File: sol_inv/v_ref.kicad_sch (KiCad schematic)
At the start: 3 parts, among them U7 LM4040DIM3-2.5, U8 MCP6001-OT

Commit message: v0.2 components change + reference to providers
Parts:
- R15: ComponentLink2URL (none) -> https://ro.farnell.com/yageo/rt0603bre078kl/res-8k-0-1-0-1w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
- U7: ComponentLink2URL (none) -> https://ro.farnell.com/texas-instruments/lm4040dim3-2-5-nop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
- U8: ComponentLink2URL (none) -> https://ro.mouser.com/ProductDetail/Microchip-Technology/MC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
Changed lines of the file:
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@@
 	(title_block
 		(title "Voltage Reference for ADC")
-		(date "2025-03-13")
-		(rev "0.1")
+		(date "2025-04-10")
+		(rev "0.2")
 		(company "Cezar-Octavian Bontaș")
 	)
@@
 			)
 		)
-		(property "Datasheet" "~"
+		(property "Datasheet" "https://www.yageo.com/upload/media/product/app/datasheet/rchip/pyu-rt_1-to-0.01_rohs_l.pdf"
 			(at 130.81 91.44 0)
 			(effects
@@
 		)
 		(property "Description" "Resistor"
+			(at 130.81 91.44 0)
+			(effects
+				(font
+					(size 1.27 1.27)
+				)
+				(hide yes)
+			)
+		)
+		(property "ComponentLink1URL" ""
+			(at 130.81 91.44 0)
+			(effects
+				(font
+					(size 1.27 1.27)
+				)
+			)
+		)
+		(property "ComponentLink2URL" "https://ro.farnell.com/yageo/rt0603bre078kl/res-8k-0-1-0-1w-thin-film-0603/dp/4148462"
 			(at 130.81 91.44 0)
 			(effects
@@
 			)
 		)
+		(property "ComponentLink1URL" ""
+			(at 130.81 106.68 0)
+			(effects
+				(font
+					(size 1.27 1.27)
+				)
+			)
+		)
+		(property "ComponentLink2URL" "https://ro.farnell.com/texas-instruments/lm4040dim3-2-5-nopb/volt-ref-shunt-2-5v-sot-23/dp/3009222"
+			(at 130.81 106.68 0)
+			(effects
+				(font
+					(size 1.27 1.27)
+				)
+				(hide yes)
+			)
+		)
 		(pin "2"
 		)
@@
 			(at 148.59 101.6 0)
 			(effects
+				(font
+					(size 1.27 1.27)
+				)
+				(hide yes)
+			)
+		)
+		(property "ComponentLink1URL" ""
+			(at 148.59 101.6 0)
+			(effects
+				(font
+					(size 1.27 1.27)
+				)
+			)
+		)
+		(property "ComponentLink2URL" "https://ro.mouser.com/ProductDetail/Microchip-Technology/MCP6001T-I-OT?qs=Q%2Fw7XRh99iki9dglS7IqJg%3D%3D"
+			(at 148.59 101.6 0)
+			(effects

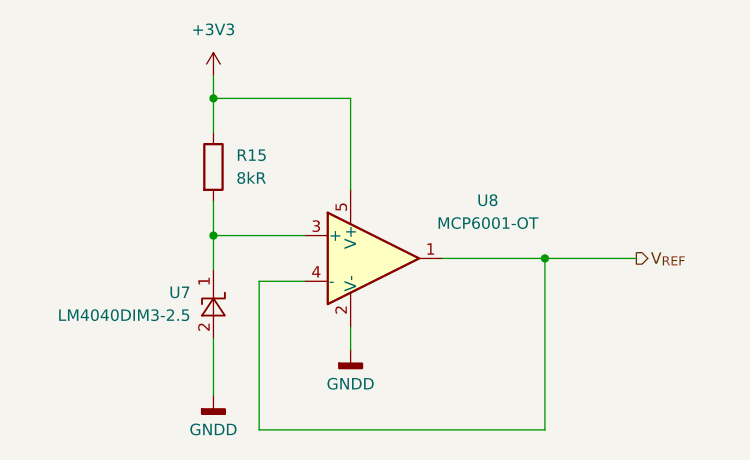
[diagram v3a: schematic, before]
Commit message: v0.3.4 fixes + component change for farnell
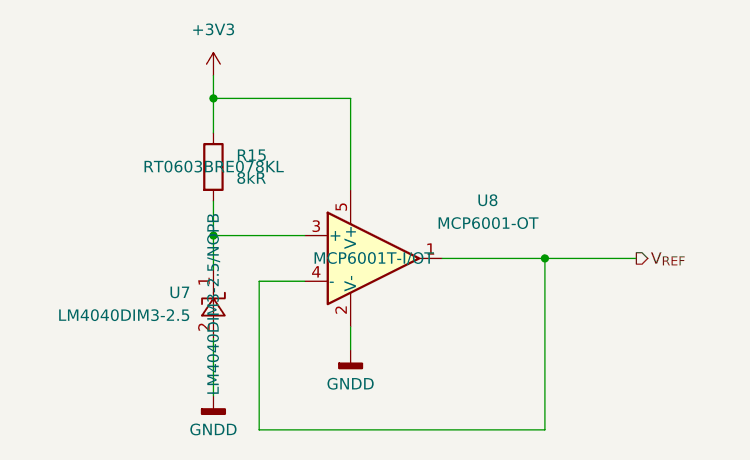
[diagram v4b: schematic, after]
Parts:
- R15: Manufacturer Part Number (none) -> RT0603BRE078KL
- U7: Manufacturer Part Number (none) -> LM4040DIM3-2.5/NOPB
- U8: Manufacturer Part Number (none) -> MCP6001T-I/OT
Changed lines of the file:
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@@
+			)
+		)
+		(property "Manufacturer Part Number" "RT0603BRE078KL"
+			(at 130.81 91.44 0)
+			(effects
+				(font
+					(size 1.27 1.27)
+				)
 			)
 		)
@@
 			)
 		)
+		(property "Manufacturer Part Number" "LM4040DIM3-2.5/NOPB"
+			(at 130.81 106.68 0)
+			(effects
+				(font
+					(size 1.27 1.27)
+				)
+			)
+		)
 		(pin "2"
 		)
@@
 			)
 		)
+		(property "Manufacturer Part Number" "MCP6001T-I/OT"
+			(at 148.59 101.6 0)
+			(effects
+				(font
+					(size 1.27 1.27)
+				)
+			)
+		)

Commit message: v0.4 fixed mcu ldo part, production testing
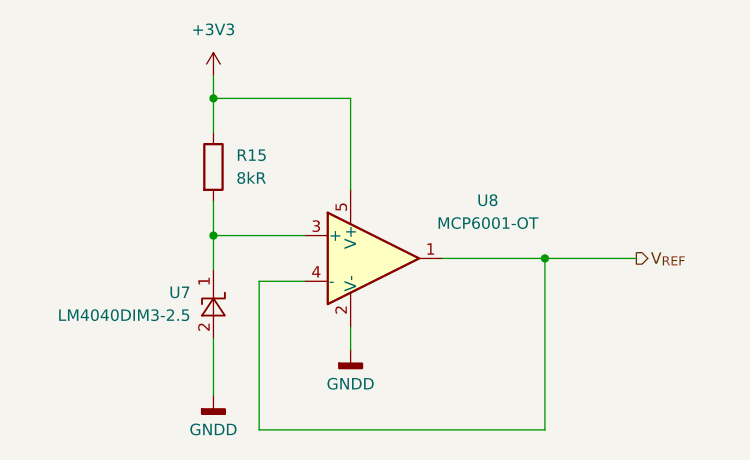
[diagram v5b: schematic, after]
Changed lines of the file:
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@@
 	(title_block
 		(title "Voltage Reference for ADC")
-		(date "2025-05-01")
-		(rev "0.3")
+		(date "2025-07-29")
+		(rev "0.4")
 		(company "Cezar-Octavian Bontaș")
 	)
@@
 					(size 1.27 1.27)
 				)
+				(hide yes)
+			)
+		)
+		(property "Sim.Enable" ""
+			(at 130.81 91.44 0)
+			(effects
+				(font
+					(size 1.27 1.27)
+				)
 			)
 		)
@@
 					(size 1.27 1.27)
 				)
+				(hide yes)
+			)
+		)
+		(property "Sim.Enable" ""
+			(at 130.81 106.68 0)
+			(effects
+				(font
+					(size 1.27 1.27)
+				)
 			)
 		)
@@
 			(at 148.59 101.6 0)
 			(effects
+				(font
+					(size 1.27 1.27)
+				)
+				(hide yes)
+			)
+		)
+		(property "Sim.Enable" ""
+			(at 148.59 101.6 0)
+			(effects
